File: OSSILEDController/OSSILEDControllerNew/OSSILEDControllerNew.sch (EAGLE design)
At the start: 77 parts, among them Q1 NX-3215, U1 OPA2347, U2 MSP430F2132, U3 LM7321, U4 MAX1682, U5 MAX890L, U6 MAX4376, U7 TPS3838, U8 MCP1700_SOT23, X1 ESQ-126-38-G-D, X2 5268-03, X3 ICCON_POWERCON, X4 ICCON_POWERCON, X5 WEIDMULLER, X6 JTAG10PINMINI-H, X7 5268-03

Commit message: gerber files are created / led current setting fixed to 9.7A
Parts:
- removed C17, C18: 12.5pF, OSSI:C0603(1608)
- removed LED3: (no value), SparkFun:LED0603
- removed R33: 1k, OSSI:R0603(1608)
- removed R63, R67: 250, OSSI:R0603(1608)
- removed R71: 10k, OSSI:R0603(1608)
- added C13: 100nF, OSSI:C0603(1608)
- added C14: 10uF, LDO Tantal 16V, OSSI:C-TANTAL-A
- added C15: 1uF 0805, OSSI:C0805(2012)
- added LED2: (no value), led:LEDCHIPLED_0603
- added R26: 1.5k, OSSI:R0603(1608)
- added R27: 0, OSSI:R0603(1608)
- added R28: TBD, OSSI:R0603(1608)
- added R29, R30: 100k, OSSI:R0603(1608)
- C1: value 1uF -> (none); device OSSI:C0603(1608) -> OSSI:C0805(2012)
- C10: value 100nF -> 10uF, LDO Tantal 16V; device OSSI:C0603(1608) -> OSSI:C-TANTAL-A
- C11: value 10uF, LDO Tantal 16V -> 1206 Cap; device OSSI:C-TANTAL-A -> OSSI:C1206(3216)-GCM31
- C12: value 10uF, LDO Tantal 16V -> 1uF; device OSSI:C-TANTAL-A -> OSSI:C0603(1608)
- C2, C4: value 100nF -> 12.5pF
- C6: value 10uF, LDO Tantal 16V -> 100nF; device OSSI:C-TANTAL-A -> OSSI:C0603(1608)
- C8: value 1uF 0805 -> 100nF; device OSSI:C0805(2012) -> OSSI:C0603(1608)
- C9: value 1206 Cap -> 10uF, LDO Tantal 16V; device OSSI:C1206(3216)-GCM31 -> OSSI:C-TANTAL-A
- LED1: device led:LEDCHIPLED_0603 -> SparkFun:LED0603
- R1: value TBD -> 511; device OSSI:R0603(1608) -> OSSI:RWSL1206
- R11: value 4.7k -> 9.1k
- R12: value 4.7k -> 1k
- R13: value 10k -> 4.7k
- R15, R20: value (none) -> 100k
- R16: value 100k -> DNP
- R17: value (none) -> 1k
- R18: value 1k -> 1.5k
- R19: value (none) -> 2.2k
- R2, R5: value 100k -> 250
- R21: value (none) -> 0.005, 2W RSENSE; device OSSI:R0603(1608) -> OSSI:RWSR2
- R22: value 0.005, 2W RSENSE -> 1.1k; device OSSI:RWSR2 -> OSSI:R0603(1608)
- R23: value 0 -> 100k
- R24: value 1.1k -> 100k
- R25: value 2.2k -> (none)
- R3, R6: value 100k -> 10k
- R7: value 1.5k -> 4.7k
- R9: value DNP -> 6.2k
- TR1: value FDD8896 -> FDV301N; device OSSI:FDD8896 -> OSSI:FDV301N
- TR2: value FDV301N -> FDD8896; device OSSI:FDV301N -> OSSI:FDD8896
- U1: value OPA2347 -> MSP430F2132; device OSSI:OPA2347 -> OSSI:MSP430F2132
- U2: value MSP430F2132 -> OPA2347; device OSSI:MSP430F2132 -> OSSI:OPA2347
- U3: value LM7321 -> MAX4376; device OSSI:LM7321 -> OSSI:MAX4376
- U4: value MAX1682 -> LM7321; device OSSI:MAX1682 -> OSSI:LM7321
- U5: value MAX890L -> MAX1682; device OSSI:MAX890L -> OSSI:MAX1682
- U6: value MAX4376 -> TPS3838; device OSSI:MAX4376 -> OSSI:TPS3838
- U7: value TPS3838 -> MAX890L; device OSSI:TPS3838 -> OSSI:MAX890L
- X3: value ICCON_POWERCON -> 5268-03; device OSSI:ICCON_POWERCON -> OSSI:5268-03
- X4: value ICCON_POWERCON -> JTAG10PINMINI-H; device OSSI:ICCON_POWERCON -> OSSI:JTAG10PINMINI-H
- X5: value WEIDMULLER -> ICCON_POWERCON; device OSSI:WEIDMULLER -> OSSI:ICCON_POWERCON
- X6: value JTAG10PINMINI-H -> ICCON_POWERCON; device OSSI:JTAG10PINMINI-H -> OSSI:ICCON_POWERCON
- X7: value 5268-03 -> WEIDMULLER; device OSSI:5268-03 -> OSSI:WEIDMULLER
- renumbered U$1 to U$
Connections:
- net 3.3VLED: now also C10.+, C5.1, C8.1, R3.2, R30.2, R6.2, U1.2, U2A.V+, U3.P$3, U6.P$5, X3.1, X4.4; no longer C10.1, C11.+, C2.1, R13.2, R2.2, R71.2, U1A.V+, U2.2, U6.P$3, U7.P$5, X2.1, X6.4
- net ACLK_OUT: now also TP1.TP, U1.8; no longer TP2.TP, U2.8
- net ADC1: now also U1.9, U2A.-IN, U2A.OUT; no longer U1A.-IN, U1A.OUT, U2.9
- net ADC2: now also U1.10, U2B.-IN, U2B.OUT; no longer U1B.-IN, U1B.OUT, U2.10
- net GND: now also C11.2, C12.2, C13.2, C14.-, C15.2, C6.2, LED2.C, R15.2, R16.2, R19.1, R22.2, R25.2, R27.2, R28.1, R29.1, TP2.TP, TR1.S, U1.4, U2A.V-, U3.P$2, U4.V-, U5.P$1, U6.P$1, U7.P$4, X2.1, X3.3, X4.9, X5.P$1, X5.P$10, X5.P$2, X5.P$3, X5.P$4, X5.P$5, X5.P$6, X5.P$7, X5.P$8, X5.P$9, X7.2; no longer C10.2, C12.-, C17.2, C18.2, C9.2, LED3.C, R17.2, R20.2, R21.2, R23.2, R25.1, R3.1, R6.2, TP3.TP, TR2.S, U1A.V-, U2.4, U3.V-, U4.P$1, U5.P$4, U7.P$1, U7.P$2, X2.3, X4.P$1, X4.P$10, X4.P$2, X4.P$3, X4.P$4, X4.P$5, X4.P$6, X4.P$7, X4.P$8, X4.P$9, X5.2, X6.9, X7.1
- net LED_-FAULT: now also U7.P$8; no longer U5.P$8
- net LED_OFF: now also C12.1, R29.2, U7.P$3; no longer C1.1, R3.2, U5.P$3
- net LED_SCL: now also R2.1, R3.1; no longer R67.1, R71.1
- net LED_SDA: now also R5.1, R6.1; no longer R13.1, R63.1
- net N$10: now also R28.2, U7.P$5; no longer R1.2, U5.P$5
- net N$11: now also R15.1, R17.2, R20.2; no longer R4.2, R5.2, R6.1
- net N$12: now also R18.1, R21.2, TP4.TP, U3.P$5, X6.P$1, X6.P$10, X6.P$2, X6.P$3, X6.P$4, X6.P$5, X6.P$6, X6.P$7, X6.P$8, X6.P$9; no longer R22.2, R7.1, TP6.TP, U6.P$5, X3.P$1, X3.P$10, X3.P$2, X3.P$3, X3.P$4, X3.P$5, X3.P$6, X3.P$7, X3.P$8, X3.P$9
- net N$13: now also C11.1, U4.V+, U5.P$2; no longer C9.1, U3.V+, U4.P$2
- net N$14: now also R19.2, R23.1, U4.OUT; no longer R16.1, R25.2, U3.OUT
- net N$15: now also U1.27, X4.3; no longer U2.27, X6.3
- net N$16: now also R21.1, TP5.TP, TR2.S, U3.P$4; no longer R22.1, TP7.TP, TR1.S, U6.P$4
- net N$17: now also C10.-, R27.1; no longer C11.-, R23.1
- net N$18: now also R22.1, U4.-IN; no longer R24.1, U3.-IN
- net N$19: now also C4.1, U1.5; no longer C17.1, U2.5
- net N$20: now also C2.1, U1.6; no longer C18.1, U2.6
- net N$21: now also LED1.A, R4.2; no longer LED3.A, R33.2
- net N$22: now also R5.2, U1.12; no longer R63.2, U2.12
- net N$23: now also R2.2, U1.13; no longer R67.2, U2.13
- net N$24: now also R11.1, U3.P$1; no longer R15.1, U6.P$1
- net N$25: now also R4.1, U1.14; no longer R33.1, U2.14
- net N$26: now also C9.-, U5.P$3; no longer C6.-, U4.P$3
- net N$27: now also C9.+, U5.P$5; no longer C6.+, U4.P$5
- net N$28: now also R8.2, U1.16; no longer R12.2, U2.16
- net N$29: now also LED2.A, R18.2; no longer LED1.A, R7.2
- net N$3: now also U1.28, X4.1; no longer U2.28, X6.1
- net N$30: now also R11.2, R9.1, TR1.G; no longer R15.2, R17.1, TR2.G
- net N$31: now also U1.26, X4.5; no longer U2.26, X6.5
- net N$32: now also R13.1, X4.10; no longer R8.1, X6.10
- net N$33: now also U1.18; no longer U2.18
- net N$39: now also R7.2, U1.15; no longer R11.2, U2.15
- net N$4: now also U1.3; no longer U2.3
- net N$5: now also C13.1, C14.+, U7.P$6, U7.P$7; no longer C12.+, C3.1, U5.P$6, U5.P$7
- net N$6: now also R16.1, R23.2, TP6.TP, TR1.D, TR2.G; no longer R16.2, R9.1, TP5.TP, TR1.G, TR2.D
- net N$7: now also C6.1, R17.1, U2A.+IN; no longer C4.1, R4.1, U1A.+IN
- net N$8: now also C3.1, R12.1, U2B.+IN; no longer C5.1, R18.1, U1B.+IN
- net N$9: now also R25.1, R26.1, U4.+IN; no longer R19.1, R21.1, U3.+IN
- net PWM: now also R24.1, R26.2; no longer R19.2, R20.1
- net RESET_LED: now also R13.2, R30.1, U1.7, U6.P$4; no longer R2.1, R8.2, U2.7, U7.P$4
- net RXD: now also R8.1, X2.3; no longer R12.1, X7.3
- net SMCLK_OUT: now also TP3.TP, U1.25, X4.7; no longer TP1.TP, U2.25, X6.7
- net STRUT_GND: now also C1.1, H4.MOUNT, R1.2; no longer H1.MOUNT
- net SUN: now also R12.2, X3.2; no longer R18.2, X2.2
- net TEST: now also U1.1, X4.8; no longer U2.1, X6.8
- net TXD: now also R7.1, X2.2; no longer R11.1, X7.2
- net VBUS: now also U7.P$1, U7.P$2; no longer U5.P$1, U5.P$2
- net VSUPERCAP: now also C15.1, R20.1, TP7.TP, TR2.D, U5.P$4, X7.1; no longer C8.1, R5.1, TP4.TP, TR1.D, U4.P$4, X5.1
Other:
- note added: "Currently set to 9.7A"
- note added: "Do Not Place Comp! Only for the EPS"
- moved on the sheet: C2, C3, C4, C5, C7, C8, H1, H2, H3, H4, LED1, R11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

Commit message: beta 1 release
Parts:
- added X8: (no value), OSSI:M03PTH
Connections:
- net GND: now also X8.3
- net LED_SCL: now also X8.2
- net LED_SDA: now also X8.1
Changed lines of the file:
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@@
 <part name="C1" library="OSSI" deviceset="C" device="0805(2012)"/>
 <part name="GND29" library="OSSI" deviceset="GND" device=""/>
+<part name="X8" library="OSSI" deviceset="M03" device="PTH"/>
+<part name="GND30" library="OSSI" deviceset="GND" device=""/>
 </parts>
 <sheets>
@@
 <instance part="TP5" gate="G$1" x="307.34" y="154.94"/>
 <instance part="U$" gate="G$1" x="27.94" y="241.3"/>
+<instance part="X8" gate="G$1" x="63.5" y="43.18" rot="MR180"/>
+<instance part="GND30" gate="1" x="73.66" y="22.86"/>
 </instances>
 <busses>
@@
 <wire x1="281.94" y1="119.38" x2="281.94" y2="121.92" width="0.1524" layer="91"/>
 </segment>
+<segment>
+<pinref part="X8" gate="G$1" pin="3"/>
+<wire x1="71.12" y1="40.64" x2="73.66" y2="40.64" width="0.1524" layer="91"/>
+<wire x1="73.66" y1="40.64" x2="73.66" y2="25.4" width="0.1524" layer="91"/>
+<pinref part="GND30" gate="1" pin="GND"/>
+</segment>
 </net>
 <net name="RESET_LED" class="0">
@@
 <pinref part="R6" gate="G$1" pin="1"/>
 <wire x1="106.68" y1="48.26" x2="106.68" y2="50.8" width="0.1524" layer="91"/>
-<wire x1="106.68" y1="48.26" x2="96.52" y2="48.26" width="0.1524" layer="91"/>
+<wire x1="106.68" y1="48.26" x2="101.6" y2="48.26" width="0.1524" layer="91"/>
 <junction x="106.68" y="48.26"/>
 <label x="96.52" y="48.26" size="1.778" layer="95" rot="R180" xref="yes"/>
+<pinref part="X8" gate="G$1" pin="1"/>
+<wire x1="101.6" y1="48.26" x2="96.52" y2="48.26" width="0.1524" layer="91"/>
+<wire x1="71.12" y1="45.72" x2="101.6" y2="45.72" width="0.1524" layer="91"/>
+<wire x1="101.6" y1="45.72" x2="101.6" y2="48.26" width="0.1524" layer="91"/>
+<junction x="101.6" y="48.26"/>
 </segment>
 </net>
@@
 <pinref part="R3" gate="G$1" pin="1"/>
 <wire x1="119.38" y1="27.94" x2="106.68" y2="27.94" width="0.1524" layer="91"/>
-<wire x1="106.68" y1="27.94" x2="96.52" y2="27.94" width="0.1524" layer="91"/>
+<wire x1="106.68" y1="27.94" x2="99.06" y2="27.94" width="0.1524" layer="91"/>
 <junction x="106.68" y="27.94"/>
 <label x="96.52" y="27.94" size="1.778" layer="95" rot="R180" xref="yes"/>
-</segment>
-</net>
+<pinref part="X8" gate="G$1" pin="2"/>
+<wire x1="99.06" y1="27.94" x2="96.52" y2="27.94" width="0.1524" layer="91"/>
+<wire x1="71.12" y1="43.18" x2="99.06" y2="43.18" width="0.1524" layer="91"/>
+<wire x1="99.06" y1="43.18" x2="99.06" y2="27.94" width="0.1524" layer="91"/>
+<junction x="99.06" y="27.94"/>
+</segment>
+</net>

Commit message: schematics renumbered
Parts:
- X3: value 5268-03 -> (none); device OSSI:5268-03 -> OSSI:M03PTH
- X4: value JTAG10PINMINI-H -> 5268-03; device OSSI:JTAG10PINMINI-H -> OSSI:5268-03
- X5: value ICCON_POWERCON -> JTAG10PINMINI-H; device OSSI:ICCON_POWERCON -> OSSI:JTAG10PINMINI-H
- X7: value WEIDMULLER -> ICCON_POWERCON; device OSSI:WEIDMULLER -> OSSI:ICCON_POWERCON
- X8: value (none) -> WEIDMULLER; device OSSI:M03PTH -> OSSI:WEIDMULLER
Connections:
- net 3.3VLED: now also X4.1, X5.4; no longer X3.1, X4.4
- net GND: now also X4.3, X5.9, X6.P$1, X6.P$10, X6.P$2, X6.P$3, X6.P$4, X6.P$5, X6.P$6, X6.P$7, X6.P$8, X6.P$9, X8.2; no longer X4.9, X5.P$1, X5.P$10, X5.P$2, X5.P$3, X5.P$4, X5.P$5, X5.P$6, X5.P$7, X5.P$8, X5.P$9, X7.2, X8.3
- net LED_SCL: now also X3.2; no longer X8.2
- net LED_SDA: now also X3.1; no longer X8.1
- net N$12: now also X7.P$1, X7.P$10, X7.P$2, X7.P$3, X7.P$4, X7.P$5, X7.P$6, X7.P$7, X7.P$8, X7.P$9; no longer X6.P$1, X6.P$10, X6.P$2, X6.P$3, X6.P$4, X6.P$5, X6.P$6, X6.P$7, X6.P$8, X6.P$9
- net N$15: now also X5.3; no longer X4.3
- net N$3: now also X5.1; no longer X4.1
- net N$31: now also X5.5; no longer X4.5
- net N$32: now also X5.10; no longer X4.10
- net SMCLK_OUT: now also X5.7; no longer X4.7
- net SUN: now also X4.2; no longer X3.2
- net TEST: now also X5.8; no longer X4.8
- net VSUPERCAP: now also X8.1; no longer X7.1
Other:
- moved on the sheet: X6

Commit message: all values for tuned results are updated
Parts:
- C11: value 1206 Cap -> 4.7uF, 1206 Cap
- R11: value 9.1k -> 5.1k
- R23: value 100k -> 1k
- R9: value 6.2k -> 3k
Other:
- note added: "Changed amp setting to comparator!!"
- note added: "Consider input bias"
- note added: "Lower Vds as much as possible"
- note added: "MOSFET Vds drop ~ 0.2V when conducts"
- note added: "Power supplied from 3.3VLED to be more predictable"
- note added: "Small Value for PWM drive"
- note added: "These resistor values has to be tuned by measuring the currents"
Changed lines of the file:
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@@
 <part name="R10" library="OSSI" deviceset="R" device="0603(1608)" value="TBD"/>
 <part name="3.3VLED1" library="OSSI" deviceset="3.3VLED" device=""/>
-<part name="R23" library="OSSI" deviceset="R" device="0603(1608)" value="100k"/>
+<part name="R23" library="OSSI" deviceset="R" device="0603(1608)" value="1k"/>
 <part name="U2" library="OSSI" deviceset="OPA2347" device=""/>
 <part name="3.3VLED3" library="OSSI" deviceset="3.3VLED" device=""/>
@@
 <part name="C15" library="OSSI" deviceset="C" device="0805(2012)" value="1uF 0805"/>
 <part name="GND16" library="OSSI" deviceset="GND" device=""/>
-<part name="C11" library="OSSI" deviceset="C" device="1206(3216)-GCM31" value="1206 Cap"/>
+<part name="C11" library="OSSI" deviceset="C" device="1206(3216)-GCM31" value="4.7uF, 1206 Cap"/>
 <part name="GND21" library="OSSI" deviceset="GND" device=""/>
 <part name="R26" library="OSSI" deviceset="R" device="0603(1608)" value="1.5k"/>
@@
 <part name="GND1" library="OSSI" deviceset="GND" device=""/>
 <part name="GND2" library="OSSI" deviceset="GND" device=""/>
-<part name="R11" library="OSSI" deviceset="R" device="0603(1608)" value="9.1k"/>
-<part name="R9" library="OSSI" deviceset="R" device="0603(1608)" value="6.2k"/>
+<part name="R11" library="OSSI" deviceset="R" device="0603(1608)" value="5.1k"/>
+<part name="R9" library="OSSI" deviceset="R" device="0603(1608)" value="3k"/>
 <part name="GND5" library="OSSI" deviceset="GND" device=""/>
 <part name="X4" library="OSSI" deviceset="5268-03" device=""/>
@@
 <text x="157.48" y="147.32" size="1.778" layer="94">Input protection needed when PWM ON, VSUPERCAP OFF</text>
 <text x="271.78" y="53.34" size="1.778" layer="94">Currently set to 9.7A</text>
+<text x="238.76" y="165.1" size="1.778" layer="94">Changed amp setting to comparator!!</text>
+<text x="228.6" y="213.36" size="1.778" layer="94">Power supplied from 3.3VLED to be more predictable</text>
+<text x="320.04" y="71.12" size="1.778" layer="94">These resistor values has to be tuned by measuring the currents</text>
+<text x="287.02" y="160.02" size="1.778" layer="94">Small Value for PWM drive</text>
+<text x="337.82" y="165.1" size="1.778" layer="94">MOSFET Vds drop ~ 0.2V when conducts</text>
+<text x="337.82" y="162.56" size="1.778" layer="94">Lower Vds as much as possible</text>
+<text x="205.74" y="139.7" size="1.778" layer="94">Consider input bias </text>
 </plain>
 <instances>

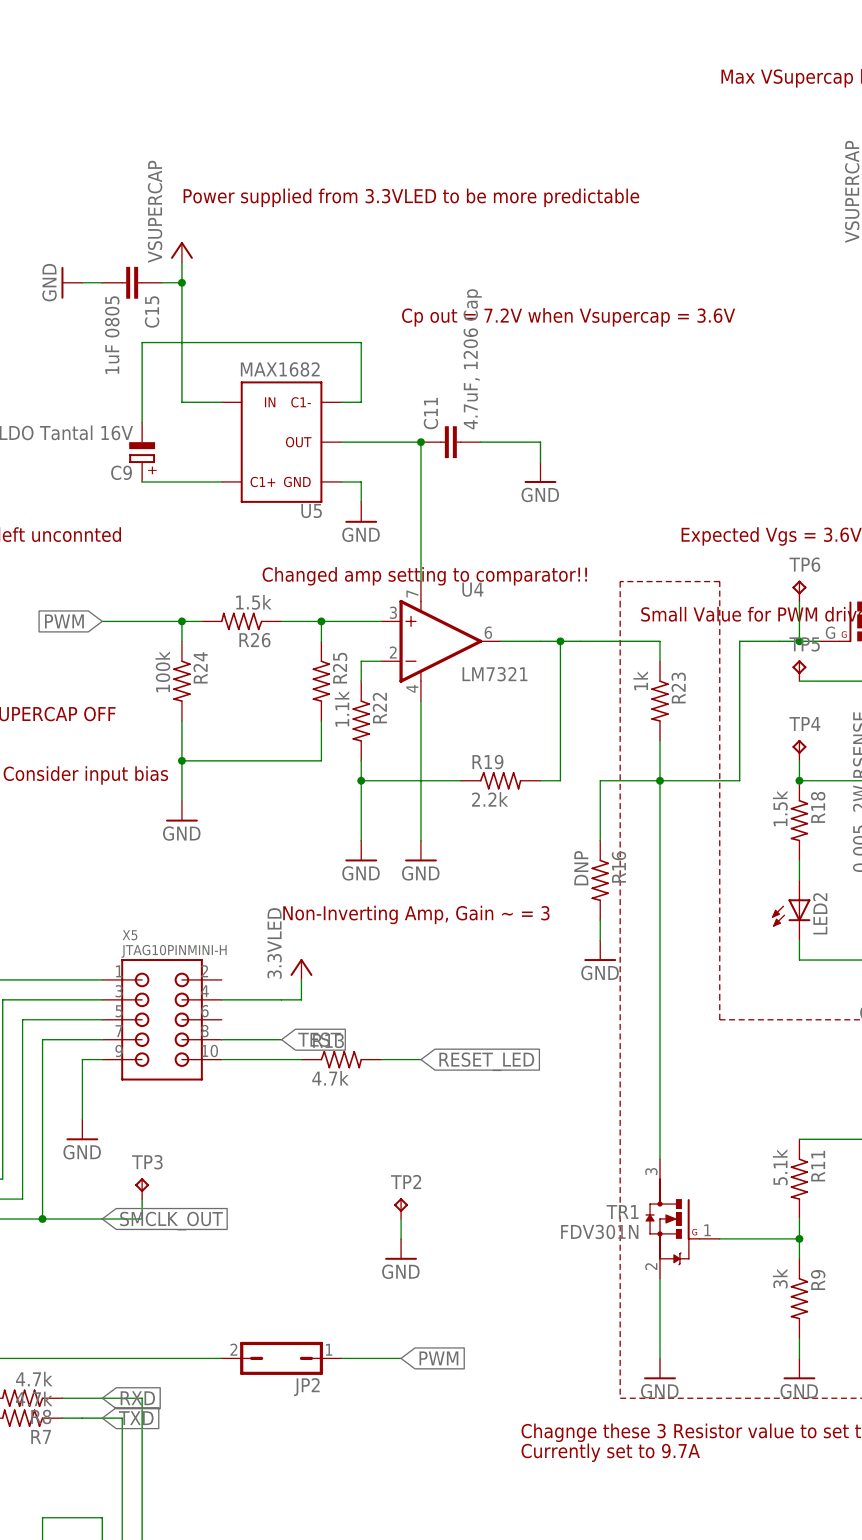
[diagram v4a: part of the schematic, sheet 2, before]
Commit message: led sch updated / design files are added
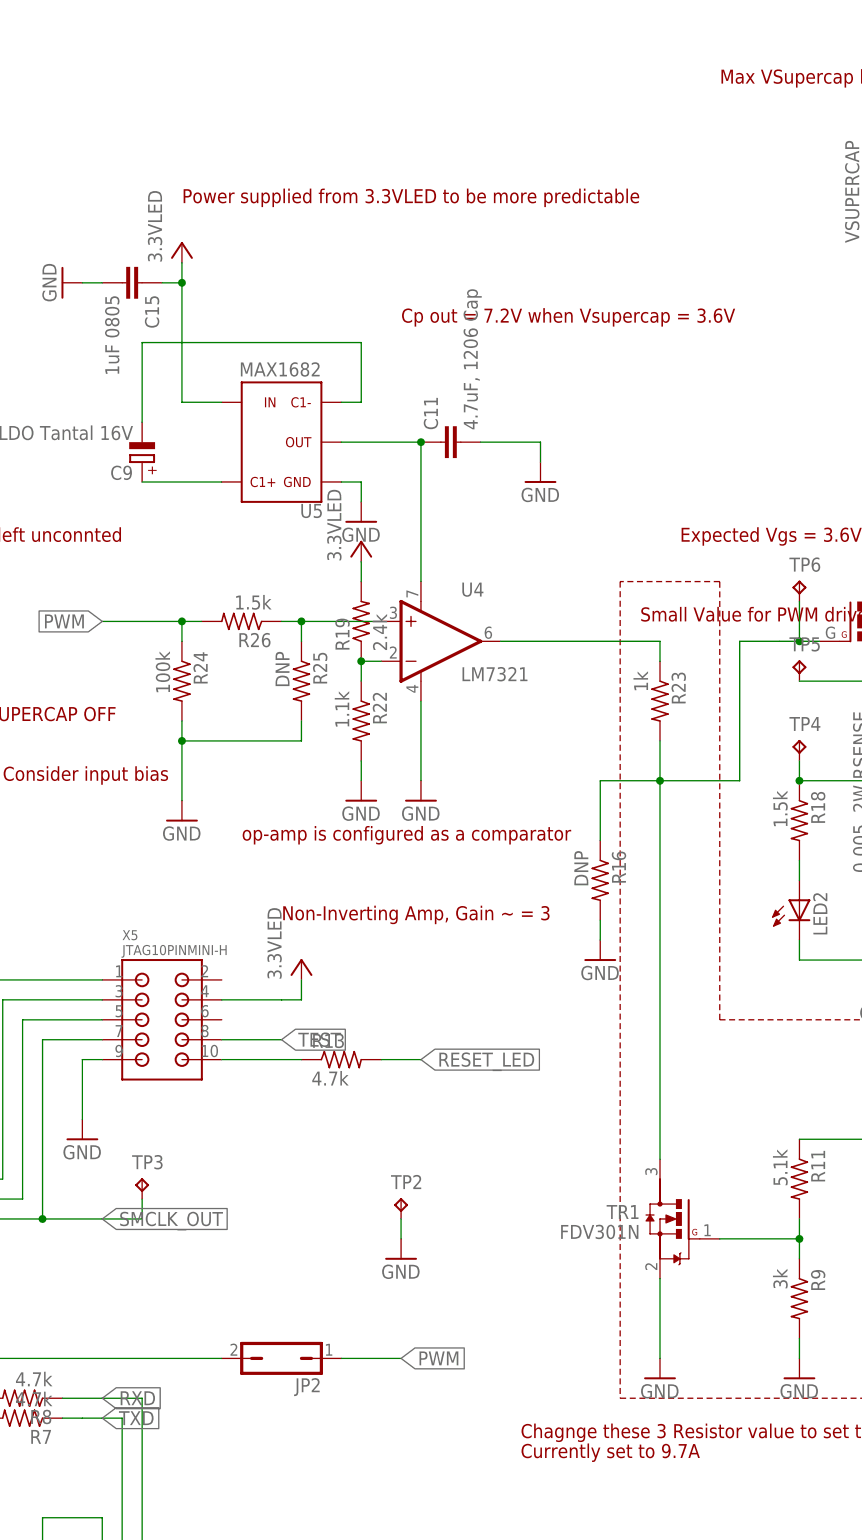
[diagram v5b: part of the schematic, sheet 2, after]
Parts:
- C1, R25: value (none) -> DNP
- R1: value 511 -> DNP
- R19: value 2.2k -> 2.4k
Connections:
- net 3.3VLED: now also C15.1, R19.2, U5.P$4
- net GND: no longer R19.1
- net N$14: no longer R19.2
- net N$18: now also R19.1
- net VSUPERCAP: no longer C15.1, U5.P$4
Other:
- note added: "Disconnect VSUPERCAP here as EPS provides measurement signal to OBC"
- note added: "op-amp is configured as a comparator"
- note removed: "Changed amp setting to comparator!!"
- note removed: "Disconnect VSUPERCAP here as EPS provide measurement signal to OBC"
- moved on the sheet: R19, R25
